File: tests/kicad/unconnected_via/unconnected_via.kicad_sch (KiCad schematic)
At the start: 2 parts

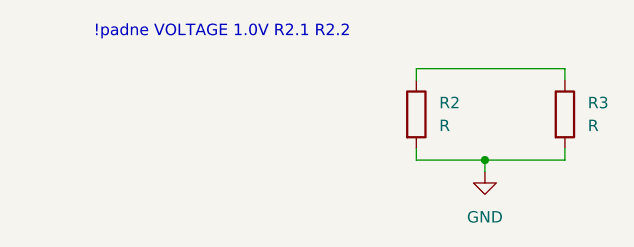
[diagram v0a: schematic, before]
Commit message: feat: Richer directive syntax
This commit adds support for named directive parameters. No more
guessing which parameter is the positive terminal positive and which is the
negative terminal!
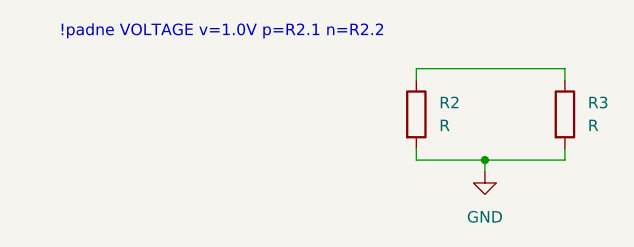
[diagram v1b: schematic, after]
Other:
- note added: "!padne VOLTAGE v=1.0V p=R2.1 n=R2.2"
- note removed: "!padne VOLTAGE 1.0V R2.1 R2.2"
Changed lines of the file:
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@@
 		)
 	)
-	(text "!padne VOLTAGE 1.0V R2.1 R2.2"
+	(text "!padne VOLTAGE v=1.0V p=R2.1 n=R2.2"
 		(exclude_from_sim no)
 		(at 118.11 96.266 0)
